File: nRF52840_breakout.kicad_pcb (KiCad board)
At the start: 4 copper layers, 27.3 x 35.9 mm, 52 parts, among them J2 Conn_ARM_JTAG_SWD_10, J3 Conn_01x22, J4 Conn_01x16, J5 Conn_01x22, J7 U.FL_A-1JB, Q1 pmos, U1 nRF52840, U2 AP2112K-3.3, U3 MCP73831-2-OT, Y1 32.768kHz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

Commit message: fixed crystal y2 90deg turn
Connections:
- Y2 pad 1: GND -> Net-(C14-Pad2)
- Y2 pad 2: Net-(C13-Pad2) -> GND
- Y2 pad 3: GND -> Net-(C13-Pad2)
- Y2 pad 4: Net-(C14-Pad2) -> GND
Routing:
- net Net-(C14-Pad2): track 8.27 -> 9.83 mm
- net Net-(C13-Pad2): track 8.19 -> 7.59 mm
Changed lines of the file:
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@@
-(kicad_pcb (version 20171130) (host pcbnew 5.1.2-f72e74a~84~ubuntu18.04.1)
+(kicad_pcb (version 20171130) (host pcbnew 5.1.4-e60b266~84~ubuntu18.04.1)
   (general
     (thickness 1.6)
     (drawings 17)
-    (tracks 706)
+    (tracks 707)
     (zones 0)
     (modules 52)
@@
     )
     (pad 4 smd rect (at -0.7 -0.55 135) (size 0.9 0.8) (layers F.Cu F.Paste F.Mask)
+      (net 2 GND))
+    (pad 3 smd rect (at 0.7 -0.55 135) (size 0.9 0.8) (layers F.Cu F.Paste F.Mask)
+      (net 9 "Net-(C13-Pad2)"))
+    (pad 2 smd rect (at 0.7 0.55 135) (size 0.9 0.8) (layers F.Cu F.Paste F.Mask)
+      (net 2 GND))
+    (pad 1 smd rect (at -0.7 0.55 135) (size 0.9 0.8) (layers F.Cu F.Paste F.Mask)
       (net 10 "Net-(C14-Pad2)"))
-    (pad 3 smd rect (at 0.7 -0.55 135) (size 0.9 0.8) (layers F.Cu F.Paste F.Mask)
-      (net 2 GND))
-    (pad 2 smd rect (at 0.7 0.55 135) (size 0.9 0.8) (layers F.Cu F.Paste F.Mask)
-      (net 9 "Net-(C13-Pad2)"))
-    (pad 1 smd rect (at -0.7 0.55 135) (size 0.9 0.8) (layers F.Cu F.Paste F.Mask)
-      (net 2 GND))
     (model ${KISYS3DMOD}/Crystal.3dshapes/Crystal_SMD_2016-4Pin_2.0x1.6mm.wrl
       (at (xyz 0 0 0))
@@
   (segment (start 112.875053 69.170732) (end 112.875053 67.277947) (width 0.145) (layer F.Cu) (net 8))
   (segment (start 112.094738 69.951047) (end 112.875053 69.170732) (width 0.145) (layer F.Cu) (net 8))
-  (segment (start 117.026034 66.667417) (end 117.010217 66.667417) (width 0.145) (layer F.Cu) (net 9))
-  (segment (start 117.026034 66.667417) (end 116.977737 66.61912) (width 0.145) (layer F.Cu) (net 9))
-  (segment (start 117.026034 66.667417) (end 117.414942 67.056325) (width 0.145) (layer F.Cu) (net 9))
+  (segment (start 116.060463 65.790931) (end 116.357447 65.493947) (width 0.145) (layer F.Cu) (net 9))
+  (segment (start 115.859309 65.992085) (end 116.060463 65.790931) (width 0.145) (layer F.Cu) (net 9))
+  (segment (start 115.859309 67.056326) (end 115.859309 65.992085) (width 0.145) (layer F.Cu) (net 9))
+  (segment (start 116.248217 67.445234) (end 115.859309 67.056326) (width 0.145) (layer F.Cu) (net 9))
+  (segment (start 113.874594 71.011708) (end 113.332174 71.011708) (width 0.145) (layer F.Cu) (net 9))
+  (segment (start 115.894664 68.991638) (end 113.874594 71.011708) (width 0.145) (layer F.Cu) (net 9))
+  (segment (start 116.248217 67.445234) (end 115.894664 67.798787) (width 0.145) (layer F.Cu) (net 9))
   (segment (start 113.332174 71.011708) (end 113.155398 71.011708) (width 0.145) (layer F.Cu) (net 9))
-  (segment (start 117.414942 67.056325) (end 117.414942 67.306558) (width 0.145) (layer F.Cu) (net 9))
-  (segment (start 113.807656 71.011708) (end 113.332174 71.011708) (width 0.145) (layer F.Cu) (net 9))
-  (segment (start 116.3447 68.474664) (end 113.807656 71.011708) (width 0.145) (layer F.Cu) (net 9))
-  (segment (start 116.3447 68.3768) (end 116.3447 68.474664) (width 0.145) (layer F.Cu) (net 9))
-  (segment (start 117.414942 67.306558) (end 116.3447 68.3768) (width 0.145) (layer F.Cu) (net 9))
-  (segment (start 116.357447 65.99883) (end 116.357447 65.493947) (width 0.145) (layer F.Cu) (net 9))
-  (segment (start 117.026034 66.667417) (end 116.357447 65.99883) (width 0.145) (layer F.Cu) (net 9))
-  (segment (start 117.802083 68.9991) (end 117.238166 68.435183) (width 0.145) (layer F.Cu) (net 10))
-  (segment (start 118.8569 68.9991) (end 117.802083 68.9991) (width 0.145) (layer F.Cu) (net 10))
-  (segment (start 115.2017 70.0278) (end 116.794317 68.435183) (width 0.145) (layer F.Cu) (net 10))
-  (segment (start 116.794317 68.435183) (end 117.238166 68.435183) (width 0.145) (layer F.Cu) (net 10))
-  (segment (start 115.2017 71.2343) (end 115.2017 70.0278) (width 0.145) (layer F.Cu) (net 10))
+  (segment (start 115.894664 67.798787) (end 115.894664 68.991638) (width 0.145) (layer F.Cu) (net 9))
+  (segment (start 118.8569 68.498283) (end 118.015983 67.657366) (width 0.145) (layer F.Cu) (net 10))
+  (segment (start 118.8569 68.9991) (end 118.8569 68.498283) (width 0.145) (layer F.Cu) (net 10))
+  (segment (start 117.460887 67.268458) (end 117.627075 67.268458) (width 0.145) (layer F.Cu) (net 10))
+  (segment (start 117.627075 67.268458) (end 118.015983 67.657366) (width 0.145) (layer F.Cu) (net 10))
+  (segment (start 116.419615 68.30973) (end 117.460887 67.268458) (width 0.145) (layer F.Cu) (net 10))
+  (segment (start 116.419615 68.880385) (end 116.419615 68.30973) (width 0.145) (layer F.Cu) (net 10))
+  (segment (start 115.2017 70.0983) (end 116.419615 68.880385) (width 0.145) (layer F.Cu) (net 10))
+  (segment (start 113.280397 71.843813) (end 113.283913 71.843813) (width 0.145) (layer F.Cu) (net 10))
+  (segment (start 115.2017 71.2343) (end 115.2017 70.0983) (width 0.145) (layer F.Cu) (net 10))
+  (segment (start 113.155398 71.718814) (end 113.280397 71.843813) (width 0.145) (layer F.Cu) (net 10))
   (segment (start 113.283913 71.843813) (end 113.4872 72.0471) (width 0.145) (layer F.Cu) (net 10))
-  (segment (start 113.280397 71.843813) (end 113.283913 71.843813) (width 0.145) (layer F.Cu) (net 10))
-  (segment (start 113.155398 71.718814) (end 113.280397 71.843813) (width 0.145) (layer F.Cu) (net 10))
+  (segment (start 113.4872 72.0471) (end 114.3889 72.0471) (width 0.145) (layer F.Cu) (net 10))
   (segment (start 114.3889 72.0471) (end 115.2017 71.2343) (width 0.145) (layer F.Cu) (net 10))
-  (segment (start 113.4872 72.0471) (end 114.3889 72.0471) (width 0.145) (layer F.Cu) (net 10))
   (segment (start 111.257053 76.305021) (end 111.257053 76.777053) (width 0.145) (layer F.Cu) (net 11))
   (segment (start 111.257053 75.618) (end 111.257053 76.305021) (width 0.145) (layer F.Cu) (net 11))

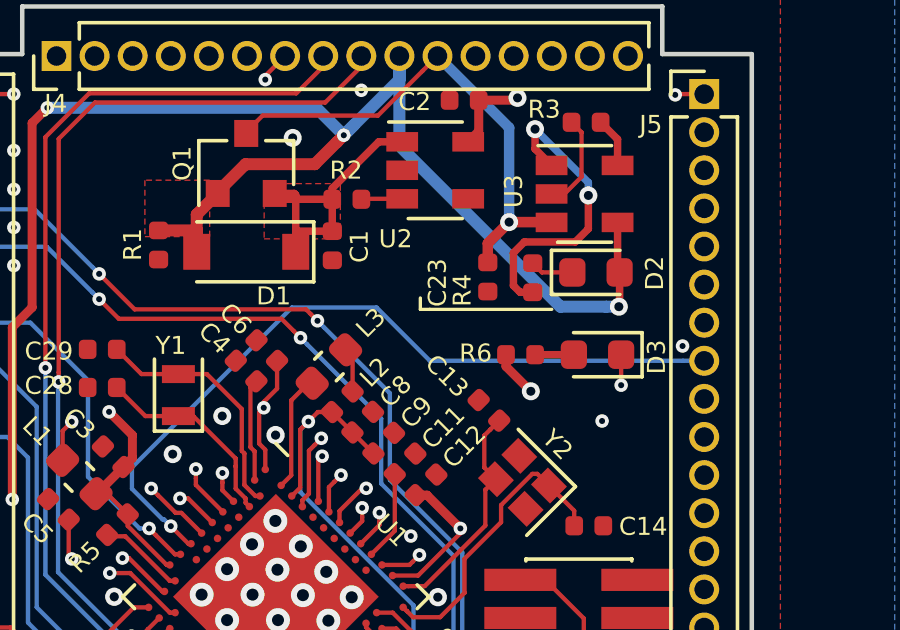
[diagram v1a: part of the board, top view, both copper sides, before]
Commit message: fixed unrouted vdd with castellated holes
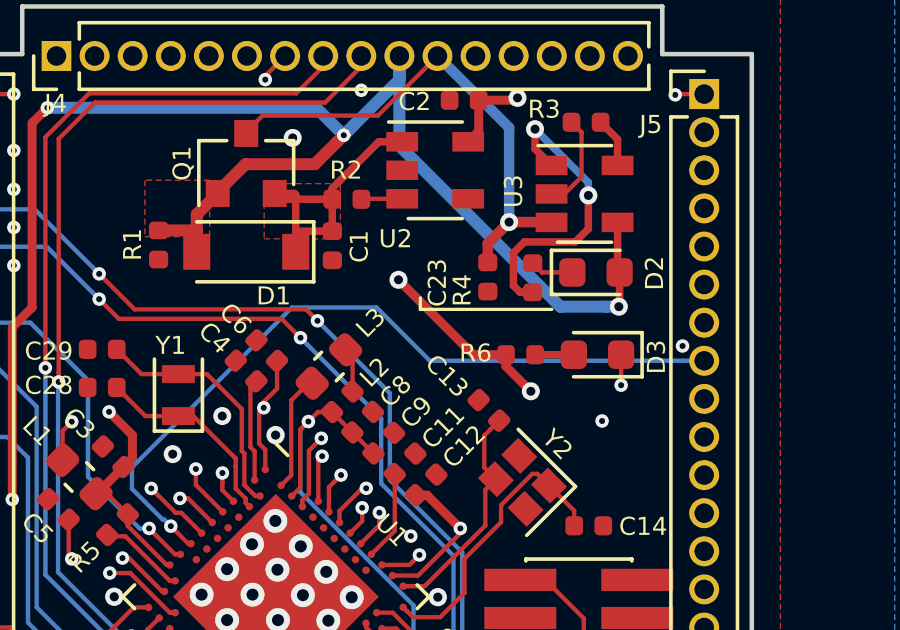
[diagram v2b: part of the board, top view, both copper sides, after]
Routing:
- net VDD_nRF: track 40.9 -> 45.5 mm, vias 9 -> 10
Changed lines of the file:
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@@
     (thickness 1.6)
     (drawings 17)
-    (tracks 707)
+    (tracks 710)
     (zones 0)
     (modules 52)
@@
   )
   (gr_line (start 100.457 53.2765) (end 100.457 51.689) (layer Edge.Cuts) (width 0.15))
+  (gr_line (start 121.793 53.2765) (end 121.793 51.689) (layer Edge.Cuts) (width 0.15))
   (gr_line (start 100.457 53.2765) (end 97.4725 53.2765) (layer Edge.Cuts) (width 0.15))
   (gr_line (start 97.4725 82.4865) (end 97.4725 53.2765) (layer Edge.Cuts) (width 0.15))
@@
   (gr_line (start 114.046 61.7855) (end 113.7285 61.7855) (layer F.SilkS) (width 0.11))
   (gr_line (start 114.046 61.7855) (end 118.11 61.7855) (layer F.SilkS) (width 0.11))
-  (gr_line (start 121.793 53.2765) (end 121.793 51.689) (layer Edge.Cuts) (width 0.15))
   (gr_line (start 121.793 53.2765) (end 124.7775 53.2765) (layer Edge.Cuts) (width 0.15))
   (gr_line (start 123.19 82.4865) (end 123.19 83.82) (layer Edge.Cuts) (width 0.15))
@@
   (segment (start 116.5836 63.2968) (end 116.5836 63.6881) (width 0.3) (layer F.Cu) (net 3))
   (segment (start 116.5836 63.6881) (end 117.4115 64.516) (width 0.3) (layer F.Cu) (net 3))
+  (via (at 113 60.8) (size 0.6) (drill 0.3) (layers F.Cu B.Cu) (net 3))
+  (segment (start 116.5836 63.2968) (end 115.4968 63.2968) (width 0.3) (layer F.Cu) (net 3))
+  (segment (start 115.4968 63.2968) (end 113 60.8) (width 0.3) (layer F.Cu) (net 3))
   (segment (start 108.065011 66.379875) (end 108.065011 64.380883) (width 0.145) (layer F.Cu) (net 4))
   (segment (start 108.065011 64.380883) (end 108.262947 64.182947) (width 0.145) (layer F.Cu) (net 4))

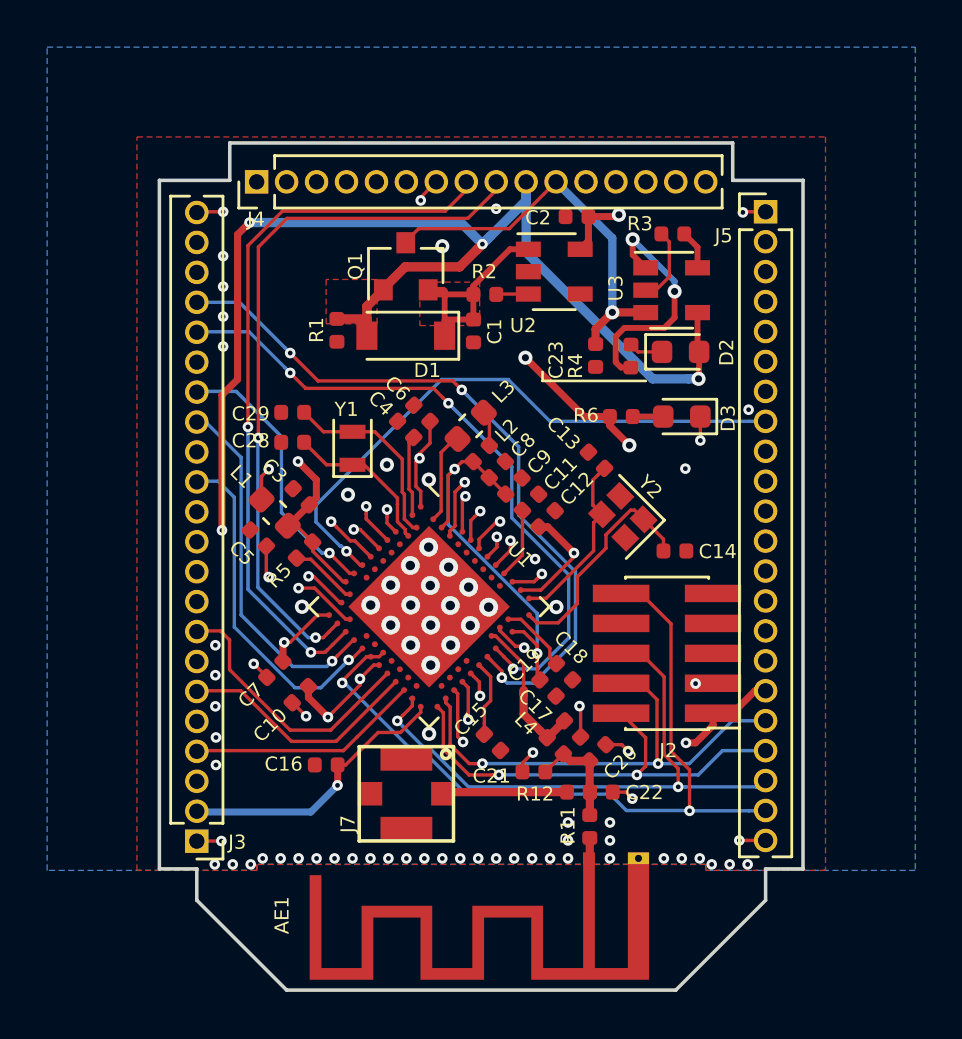
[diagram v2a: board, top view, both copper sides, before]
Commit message: added keepout and edited edge cuts
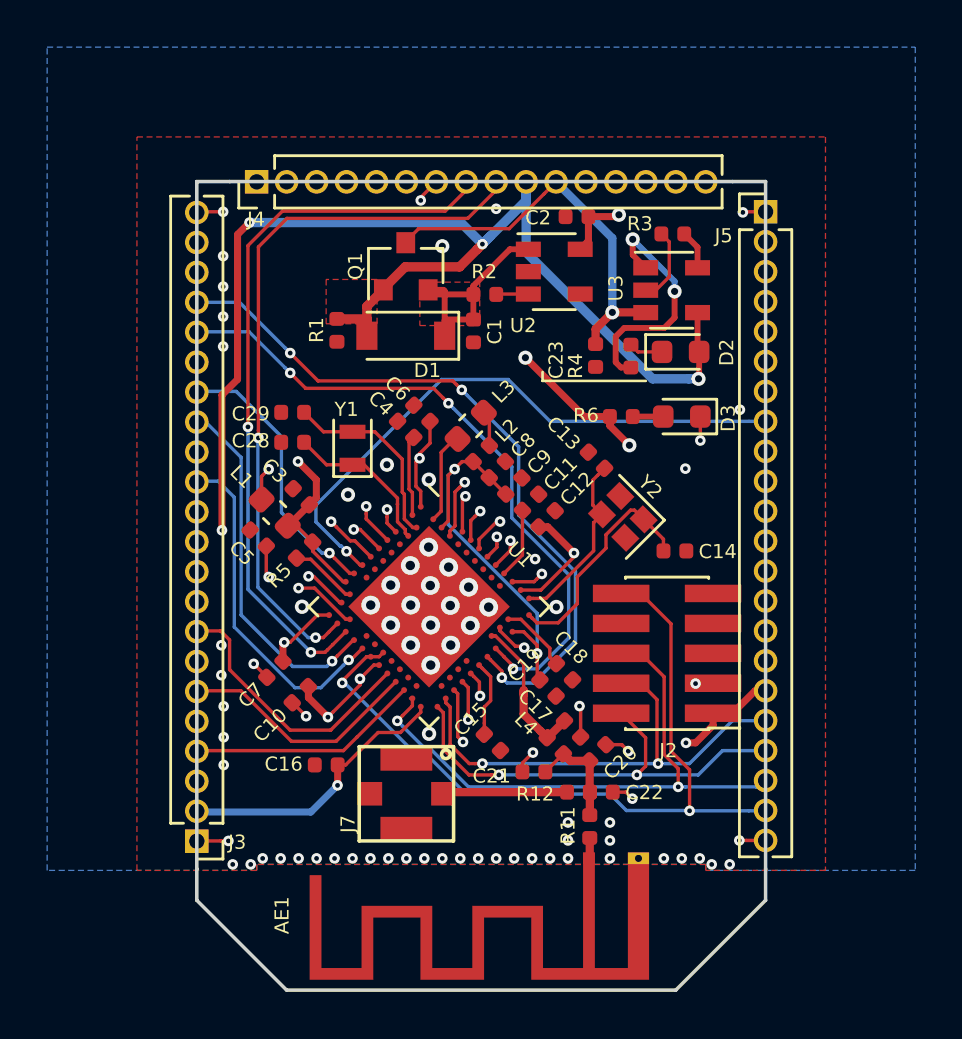
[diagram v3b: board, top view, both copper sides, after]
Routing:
- net GND: track 14.4 -> 14.7 mm, vias 83 -> 81
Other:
- board size 27.3 x 35.9 mm -> 24.1 x 34.3 mm
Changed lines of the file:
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@@
-(kicad_pcb (version 20171130) (host pcbnew 5.1.4-e60b266~84~ubuntu18.04.1)
+(kicad_pcb (version 20171130) (host pcbnew 5.1.5-52549c5~84~ubuntu18.04.1)
   (general
     (thickness 1.6)
-    (drawings 17)
+    (drawings 13)
     (tracks 710)
     (zones 0)
@@
     (visible_elements FFFFFF7F)
     (pcbplotparams
-      (layerselection 0x010fc_ffffffff)
+      (layerselection 0x3f0fc_ffffffff)
       (usegerberextensions false)
       (usegerberattributes false)
@@
     )
   )
-  (gr_line (start 100.457 53.2765) (end 100.457 51.689) (layer Edge.Cuts) (width 0.15))
-  (gr_line (start 121.793 53.2765) (end 121.793 51.689) (layer Edge.Cuts) (width 0.15))
-  (gr_line (start 100.457 53.2765) (end 97.4725 53.2765) (layer Edge.Cuts) (width 0.15))
-  (gr_line (start 97.4725 82.4865) (end 97.4725 53.2765) (layer Edge.Cuts) (width 0.15))
+  (gr_line (start 100.457 53.3273) (end 99.06 53.3273) (layer Edge.Cuts) (width 0.15))
+  (gr_line (start 99.06 82.4865) (end 99.06 53.3273) (layer Edge.Cuts) (width 0.15))
   (gr_line (start 99.06 82.4865) (end 99.06 83.82) (layer Edge.Cuts) (width 0.15))
   (gr_line (start 113.7285 61.7855) (end 113.7285 61.4045) (layer F.SilkS) (width 0.11))
   (gr_line (start 114.046 61.7855) (end 113.7285 61.7855) (layer F.SilkS) (width 0.11))
   (gr_line (start 114.046 61.7855) (end 118.11 61.7855) (layer F.SilkS) (width 0.11))
-  (gr_line (start 121.793 53.2765) (end 124.7775 53.2765) (layer Edge.Cuts) (width 0.15))
+  (gr_line (start 121.793 53.3273) (end 123.19 53.3273) (layer Edge.Cuts) (width 0.15))
   (gr_line (start 123.19 82.4865) (end 123.19 83.82) (layer Edge.Cuts) (width 0.15))
-  (gr_line (start 99.06 82.4865) (end 97.4725 82.4865) (layer Edge.Cuts) (width 0.15))
-  (gr_line (start 121.793 51.689) (end 100.457 51.689) (layer Edge.Cuts) (width 0.15))
-  (gr_line (start 124.7775 82.4865) (end 124.7775 53.2765) (layer Edge.Cuts) (width 0.15))
-  (gr_line (start 123.19 82.4865) (end 124.7775 82.4865) (layer Edge.Cuts) (width 0.15))
+  (gr_line (start 121.793 53.3273) (end 100.457 53.3273) (layer Edge.Cuts) (width 0.15))
+  (gr_line (start 123.19 82.4865) (end 123.19 53.3273) (layer Edge.Cuts) (width 0.15))
   (gr_line (start 123.19 83.82) (end 119.38 87.63) (layer Edge.Cuts) (width 0.15))
   (gr_line (start 99.06 83.82) (end 102.87 87.63) (layer Edge.Cuts) (width 0.15))
@@
   (via (at 100.1776 56.4896) (size 0.45) (drill 0.2) (layers F.Cu B.Cu) (net 2))
   (via (at 119.7864 65.5066) (size 0.45) (drill 0.2) (layers F.Cu B.Cu) (net 2))
-  (via (at 99.8474 72.9996) (size 0.45) (drill 0.2) (layers F.Cu B.Cu) (net 2))
-  (via (at 99.8474 74.2696) (size 0.45) (drill 0.2) (layers F.Cu B.Cu) (net 2))
-  (via (at 99.8474 75.5904) (size 0.45) (drill 0.2) (layers F.Cu B.Cu) (net 2))
-  (via (at 99.8728 76.9112) (size 0.45) (drill 0.2) (layers F.Cu B.Cu) (net 2))
-  (via (at 99.8728 78.0796) (size 0.45) (drill 0.2) (layers F.Cu B.Cu) (net 2))
-  (via (at 100.1014 81.3054) (size 0.45) (drill 0.2) (layers F.Cu B.Cu) (net 2))
-  (segment (start 100.1014 81.3054) (end 99.40751 81.3054) (width 0.145) (layer F.Cu) (net 2))
+  (via (at 100.1 72.9996) (size 0.45) (drill 0.2) (layers F.Cu B.Cu) (net 2))
+  (via (at 100.1 74.2696) (size 0.45) (drill 0.2) (layers F.Cu B.Cu) (net 2))
+  (via (at 100.2 75.5904) (size 0.45) (drill 0.2) (layers F.Cu B.Cu) (net 2))
+  (via (at 100.2 76.9) (size 0.45) (drill 0.2) (layers F.Cu B.Cu) (net 2))
+  (via (at 100.2 78.0796) (size 0.45) (drill 0.2) (layers F.Cu B.Cu) (net 2))
   (via (at 100.1776 54.61) (size 0.45) (drill 0.2) (layers F.Cu B.Cu) (net 2))
   (via (at 122.2248 54.6354) (size 0.45) (drill 0.2) (layers F.Cu B.Cu) (net 2))
@@
   (via (at 120.904 82.296) (size 0.45) (drill 0.2) (layers F.Cu B.Cu) (net 2))
   (via (at 121.666 82.296) (size 0.45) (drill 0.2) (layers F.Cu B.Cu) (net 2))
-  (via (at 122.428 82.296) (size 0.45) (drill 0.2) (layers F.Cu B.Cu) (net 2))
   (via (at 100.584 82.296) (size 0.45) (drill 0.2) (layers F.Cu B.Cu) (net 2))
-  (via (at 99.822 82.296) (size 0.45) (drill 0.2) (layers F.Cu B.Cu) (net 2))
   (via (at 116.586 82.042) (size 0.45) (drill 0.2) (layers F.Cu B.Cu) (net 2))
   (via (at 118.872 82.042) (size 0.45) (drill 0.2) (layers F.Cu B.Cu) (net 2))
@@
   (segment (start 103.10741 75.438196) (end 103.124196 75.438196) (width 0.145) (layer F.Cu) (net 2))
   (segment (start 103.124196 75.438196) (end 103.6955 76.0095) (width 0.145) (layer F.Cu) (net 2))
-  (via (at 122.46864 63.00724) (size 0.45) (drill 0.2) (layers F.Cu B.Cu) (net 2))
+  (via (at 122.1 63.00724) (size 0.45) (drill 0.2) (layers F.Cu B.Cu) (net 2))
   (segment (start 120.4215 63.2968) (end 120.4215 64.3127) (width 0.145) (layer F.Cu) (net 2))
   (via (at 120.4214 64.3128) (size 0.45) (drill 0.2) (layers F.Cu B.Cu) (net 2))
@@
   (via (at 113.411 69.342) (size 0.45) (drill 0.2) (layers F.Cu B.Cu) (net 2))
   (via (at 111.76 54.483) (size 0.45) (drill 0.2) (layers F.Cu B.Cu) (net 2))
+  (segment (start 99.41291 81.3) (end 100.081802 81.3) (width 0.145) (layer F.Cu) (net 2))
+  (segment (start 99.40751 81.3054) (end 99.41291 81.3) (width 0.145) (layer F.Cu) (net 2))
+  (via (at 100.4 81.3) (size 0.45) (drill 0.2) (layers F.Cu B.Cu) (net 2))
+  (segment (start 100.081802 81.3) (end 100.4 81.3) (width 0.145) (layer F.Cu) (net 2))
   (segment (start 103.139447 67.782553) (end 103.974947 68.618053) (width 0.145) (layer F.Cu) (net 3))
   (segment (start 103.139447 67.735947) (end 103.139447 67.782553) (width 0.145) (layer F.Cu) (net 3))
@@
       )
     )
+  )
+  (zone (net 0) (net_name "") (layers F.Cu In1.Cu In2.Cu B.Cu) (hatch edge 0.508)
+    (connect_pads (clearance 0.13))
+    (min_thickness 0.254)
+    (keepout (tracks allowed) (vias allowed) (copperpour not_allowed))
+    (fill (arc_segments 32) (thermal_gap 0.508) (thermal_bridge_width 0.508))
+    (polygon
+      (pts
+        (xy 99.8 82.5) (xy 98.3 82.5) (xy 98.3 53.1) (xy 99.8 53.1)
+      )
+    )
+  )
+  (zone (net 0) (net_name "") (layers F.Cu In1.Cu In2.Cu B.Cu) (hatch edge 0.508)
+    (connect_pads (clearance 0.13))
+    (min_thickness 0.254)
+    (keepout (tracks allowed) (vias allowed) (copperpour not_allowed))
+    (fill (arc_segments 32) (thermal_gap 0.508) (thermal_bridge_width 0.508))
+    (polygon
+      (pts
+        (xy 122.5 54.1) (xy 99.8 54.1) (xy 99.8 52.6) (xy 122.5 52.6)
+      )
+    )
+  )
+  (zone (net 0) (net_name "") (layers F.Cu In1.Cu In2.Cu B.Cu) (hatch edge 0.508)
+    (connect_pads (clearance 0.13))
+    (min_thickness 0.254)
+    (keepout (tracks allowed) (vias allowed) (copperpour not_allowed))
+    (fill (arc_segments 32) (thermal_gap 0.508) (thermal_bridge_width 0.508))
+    (polygon
+      (pts
+        (xy 123.9 82.6) (xy 122.5 82.6) (xy 122.5 53.1) (xy 123.9 53.1)
+      )
+    )

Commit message: add missing gnd to charge ic
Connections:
- R3 pad 1: Net-(R3-Pad1) -> GND
- U3 pad 2: Net-(R3-Pad1) -> GND
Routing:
- net GND: track 14.7 -> 17.9 mm
- net Net-(R3-Pad1): track 3.19 -> 0.00 mm
